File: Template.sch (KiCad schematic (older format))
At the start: 15 parts, among them T1 BC847

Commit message: Testowa zmiana schematu i plytki
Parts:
- added J1: Z, _obudowy:TACT_3x2.4_SMD, symbol Z
- added R2: R, _obudowy:R_1206, symbol R
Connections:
- net 5V: now also J1.2
- net GND: now also R2.2; no longer R1.1
- new net: J1.1, R1.1, R2.1
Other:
- moved on the sheet: D1
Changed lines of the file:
@@
 encoding utf-8
 Sheet 1 1
-Title "GitHub Test"
+Title "Template"
 Date "2020.01.16"
 Rev "100"
@@
 L 5V #PWR016
 U 1 1 5F93467C
-P 5500 3000
-F 0 "#PWR016" H 5500 3100 30  0001 C CNN
-F 1 "5V" H 5500 3100 30  0000 C CNN
-F 2 "" H 5500 3000 60  0000 C CNN
-F 3 "" H 5500 3000 60  0000 C CNN
-	1    5500 3000
+P 5500 3150
+F 0 "#PWR016" H 5500 3250 30  0001 C CNN
+F 1 "5V" H 5500 3250 30  0000 C CNN
+F 2 "" H 5500 3150 60  0000 C CNN
+F 3 "" H 5500 3150 60  0000 C CNN
+	1    5500 3150
 	1    0    0    -1
 $EndComp
@@
 L GND #PWR017
 U 1 1 5F93478F
-P 5500 3850
-F 0 "#PWR017" H 5500 3850 30  0001 C CNN
-F 1 "GND" H 5500 3780 30  0001 C CNN
-F 2 "" H 5500 3850 60  0000 C CNN
-F 3 "" H 5500 3850 60  0000 C CNN
-	1    5500 3850
+P 5500 4200
+F 0 "#PWR017" H 5500 4200 30  0001 C CNN
+F 1 "GND" H 5500 4130 30  0001 C CNN
+F 2 "" H 5500 4200 60  0000 C CNN
+F 3 "" H 5500 4200 60  0000 C CNN
+	1    5500 4200
 	1    0    0    -1
 $EndComp
@@
 L LED D1
 U 1 1 5F93487B
-P 5500 3250
-F 0 "D1" H 5500 3350 50  0000 C CNN
-F 1 "LED" H 5420 3150 40  0000 C CNN
-F 2 "_obudowy:LED_1206" H 5400 3250 60  0001 C CNN
-F 3 "" H 5500 3350 60  0000 C CNN
-	1    5500 3250
+P 5500 3300
+F 0 "D1" H 5500 3400 50  0000 C CNN
+F 1 "LED" H 5420 3200 40  0000 C CNN
+F 2 "_obudowy:LED_1206" H 5400 3300 60  0001 C CNN
+F 3 "" H 5500 3400 60  0000 C CNN
+	1    5500 3300
 	0    1    1    0
 $EndComp
@@
 $EndComp
 Wire Wire Line
-	5500 3000 5500 3150
-Wire Wire Line
-	5500 3350 5500 3450
-Wire Wire Line
-	5500 3800 5500 3750
+	5500 3150 5500 3200
+Wire Wire Line
+	5500 3400 5500 3450
+Wire Wire Line
+	5500 3750 5500 4150
 Wire Wire Line
 	5300 3600 5200 3600
@@
 L GND #PWR018
 U 1 1 5F933F00
-P 4800 3850
-F 0 "#PWR018" H 4800 3850 30  0001 C CNN
-F 1 "GND" H 4800 3780 30  0001 C CNN
-F 2 "" H 4800 3850 60  0000 C CNN
-F 3 "" H 4800 3850 60  0000 C CNN
-	1    4800 3850
-	1    0    0    -1
-$EndComp
-Wire Wire Line
-	4800 3800 4800 3600
+P 4800 4200
+F 0 "#PWR018" H 4800 4200 30  0001 C CNN
+F 1 "GND" H 4800 4130 30  0001 C CNN
+F 2 "" H 4800 4200 60  0000 C CNN
+F 3 "" H 4800 4200 60  0000 C CNN
+	1    4800 4200
+	1    0    0    -1
+$EndComp
 Wire Wire Line
 	4800 3600 4900 3600
+$Comp
+L Z J1
+U 1 1 5F93471D
+P 4800 3350
+F 0 "J1" H 4750 3300 40  0000 C CNN
+F 1 "Z" H 4865 3300 40  0000 C CNN
+F 2 "_obudowy:TACT_3x2.4_SMD" H 4800 3350 60  0001 C CNN
+F 3 "" H 4800 3350 60  0000 C CNN
+	1    4800 3350
+	0    -1   1    0
+$EndComp
+$Comp
+L R R2
+U 1 1 5F934800
+P 4800 3900
+F 0 "R2" V 4885 3900 50  0000 C CNN
+F 1 "R" V 4800 3900 35  0000 C CNN
+F 2 "_obudowy:R_1206" V 4785 3800 60  0001 C CNN
+F 3 "" H 4800 3900 60  0000 C CNN
+	1    4800 3900
+	-1   0    0    -1
+$EndComp
+$Comp
+L 5V #PWR019
+U 1 1 5F93485B
+P 4800 3150
+F 0 "#PWR019" H 4800 3250 30  0001 C CNN
+F 1 "5V" H 4800 3250 30  0000 C CNN
+F 2 "" H 4800 3150 60  0000 C CNN
+F 3 "" H 4800 3150 60  0000 C CNN
+	1    4800 3150
+	1    0    0    -1
+$EndComp
+Wire Wire Line
+	4800 3150 4800 3250
+Wire Wire Line
+	4800 3450 4800 3750
+Connection ~ 4800 3600
+Wire Wire Line
+	4800 4050 4800 4150
 $EndSCHEMATC

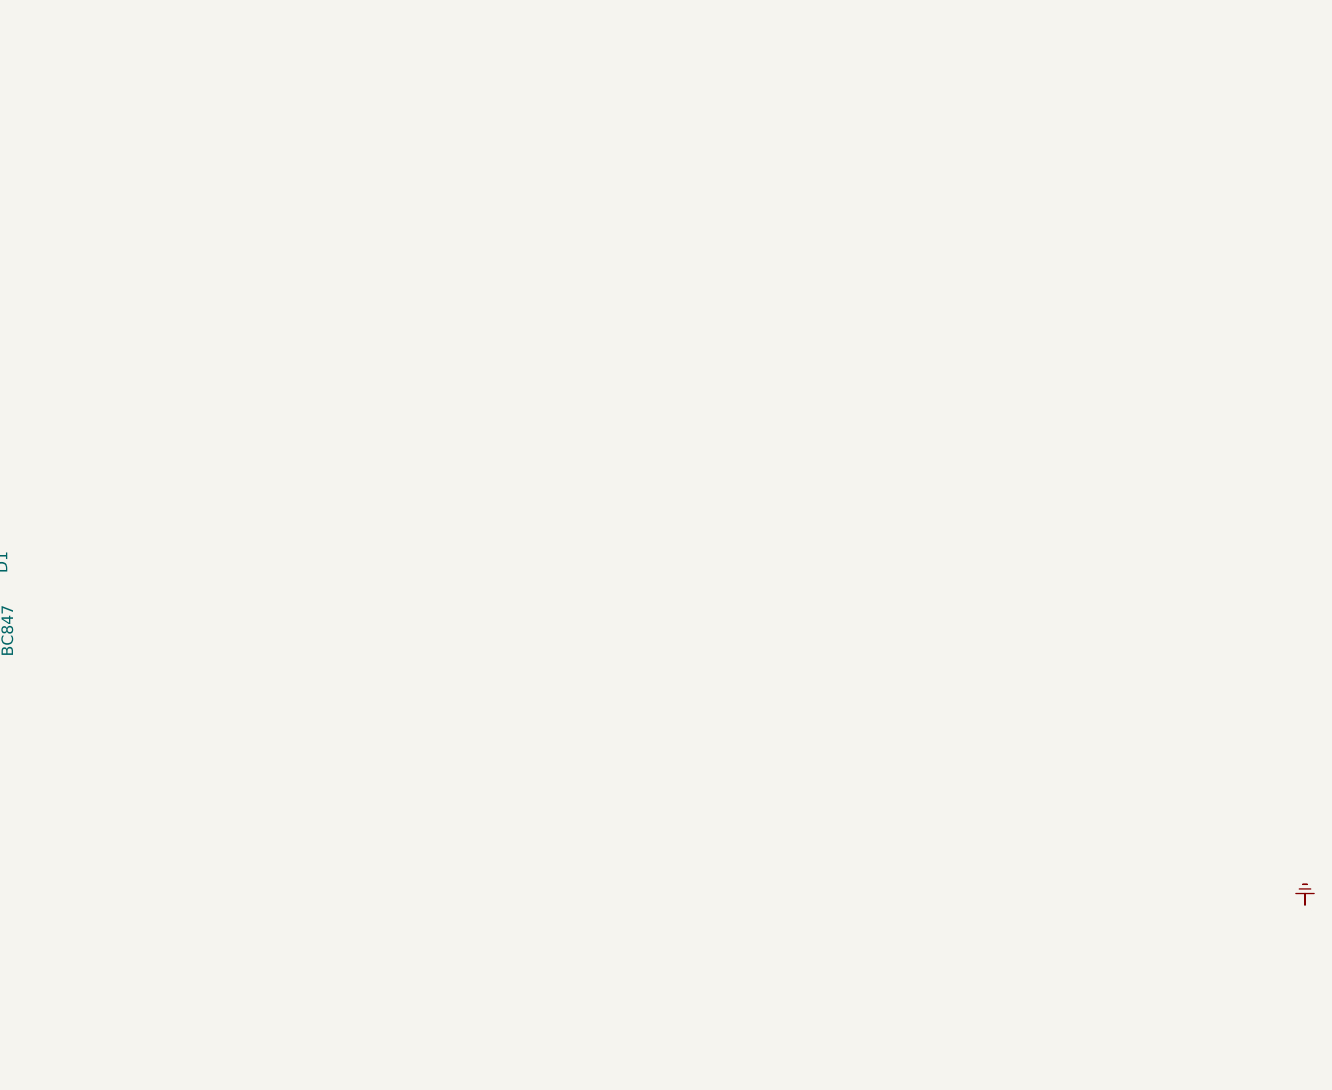
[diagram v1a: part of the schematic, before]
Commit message: Added ESP32-WROOM
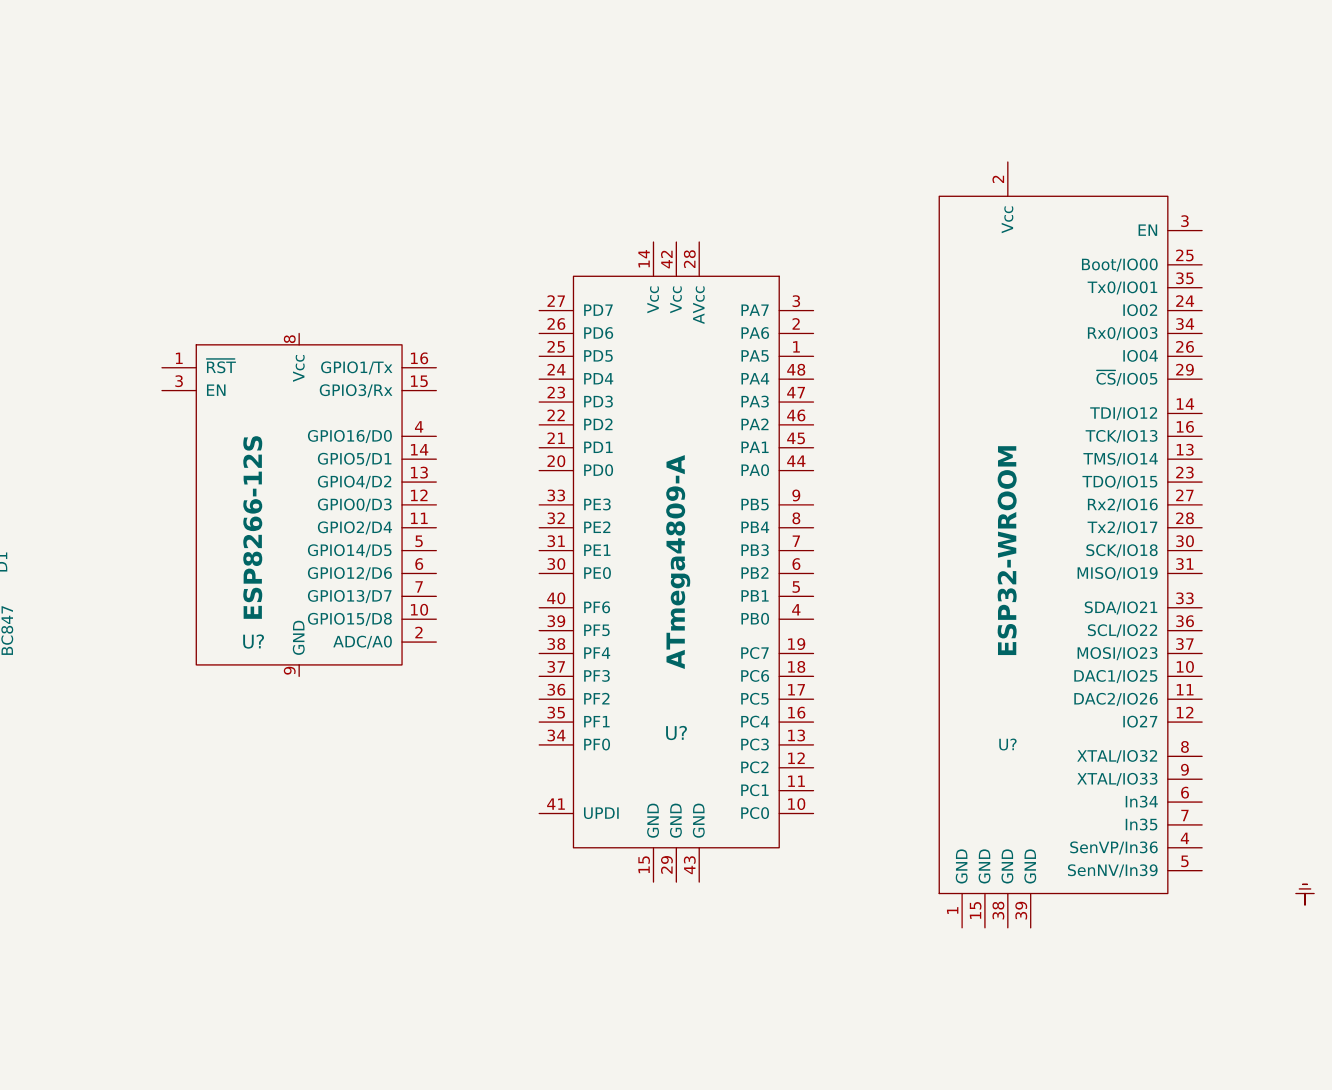
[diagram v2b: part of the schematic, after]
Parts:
- added U?: ESP8266-12S, symbol ESP8266-12S
- added U?: ATmega4809-A, symbol ATmega4809-A
- added U?: ESP32-WROOM, _obudowy:ESP32-WROOM-32E, symbol ESP32-WROOM
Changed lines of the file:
@@
 Wire Wire Line
 	4800 4050 4800 4150
+$Comp
+L ESP8266-12S U?
+U 1 1 5F93FE14
+P 6900 2950
+F 0 "U?" H 6700 2250 60  0000 C CNN
+F 1 "ESP8266-12S" V 6700 2750 80  0000 C CNB
+F 2 "" H 6900 2950 60  0001 C CNN
+F 3 "" H 6900 2950 60  0001 C CNN
+	1    6900 2950
+	1    0    0    -1
+$EndComp
+$Comp
+L ATmega4809-A U?
+U 1 1 5F93FF7D
+P 8550 3300
+F 0 "U?" H 8550 2550 60  0000 C CNN
+F 1 "ATmega4809-A" V 8550 3300 80  0000 C CNB
+F 2 "" H 8550 2075 25  0001 C CNN
+F 3 "" H 8850 2850 60  0001 C CNN
+	1    8550 3300
+	1    0    0    -1
+$EndComp
+$Comp
+L ESP32-WROOM U?
+U 1 1 5F944174
+P 10000 3250
+F 0 "U?" H 10000 2400 50  0000 C CNN
+F 1 "ESP32-WROOM" V 10000 3250 80  0000 C CNB
+F 2 "_obudowy:ESP32-WROOM-32E" V 9800 3250 50  0001 C CNN
+F 3 "" H 10000 3200 50  0001 C CNN
+	1    10000 3250
+	1    0    0    -1
+$EndComp
 $EndSCHEMATC
